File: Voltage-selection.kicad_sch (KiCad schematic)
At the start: 15 parts, among them Q3 DMP1045U-7, Q4 DMP1045U-7, Q5 DMP1045U-7, SW4 6V 300mA

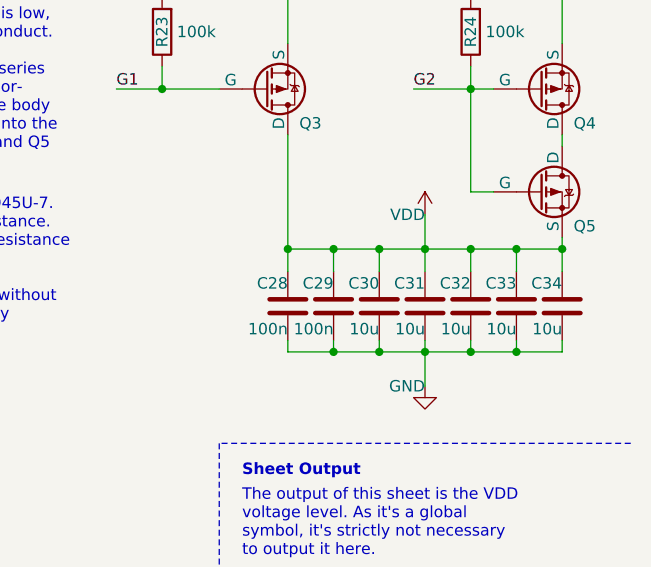
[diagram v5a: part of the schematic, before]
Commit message: Rename capacitors
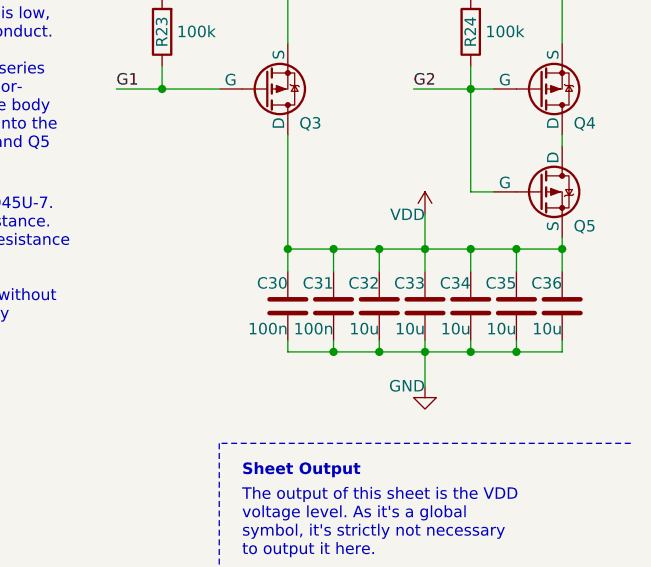
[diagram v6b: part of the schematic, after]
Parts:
- C30: renamed from C28; Comment (none) -> 16V 100nF X7R ±10% 0402
- C31: renamed from C29; Comment (none) -> 16V 100nF X7R ±10% 0402
- C32: renamed from C30; Comment (none) -> 25V 10uF X5R ±10% 0805
- C33: renamed from C31; Comment (none) -> 25V 10uF X5R ±10% 0805
- C34: renamed from C32; Comment (none) -> 25V 10uF X5R ±10% 0805
- C35: renamed from C33; Comment (none) -> 25V 10uF X5R ±10% 0805
- C36: renamed from C34; Comment (none) -> 25V 10uF X5R ±10% 0805
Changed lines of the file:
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@@
   (symbol (lib_id "Device:C") (at 179.07 62.23 0) (mirror y) (unit 1)
     (in_bom yes) (on_board yes) (dnp no)
-    (property "Reference" "C32" (at 179.07 59.69 0)
+    (property "Reference" "C34" (at 179.07 59.69 0)
       (effects (font (size 1.27 1.27)) (justify left))
     )
@@
       (effects (font (size 1.27 1.27)) hide)
     )
+    (property "Comment" "25V 10uF X5R ±10% 0805" (at 179.07 62.23 0)
+      (effects (font (size 1.27 1.27)) hide)
+    )
+    (pin "1")
+    (pin "2")
+    (instances
+      (project "tiny-scarab"
+        (path "/156c5422-ee07-49a4-8263-a2dbd26b90bd/481ed0a2-b40b-451f-8f8b-138317026240"
+          (reference "C34") (unit 1)
+        )
+      )
+    )
+  )
+  (symbol (lib_id "Device:C") (at 168.91 62.23 0) (mirror y) (unit 1)
+    (in_bom yes) (on_board yes) (dnp no)
+    (property "Reference" "C32" (at 168.91 59.69 0)
+      (effects (font (size 1.27 1.27)) (justify left))
+    )
+    (property "Value" "10u" (at 168.91 64.77 0)
+      (effects (font (size 1.27 1.27)) (justify left))
+    )
+    (property "Footprint" "Capacitor_SMD:C_0805_2012Metric" (at 167.9448 66.04 0)
+      (effects (font (size 1.27 1.27)) hide)
+    )
+    (property "Datasheet" "~" (at 168.91 62.23 0)
+      (effects (font (size 1.27 1.27)) hide)
+    )
+    (property "Manufacturer" "Samsung electro-mechanics" (at 168.91 62.23 0)
+      (effects (font (size 1.27 1.27)) hide)
+    )
+    (property "MPN" "CL21A106KAYNNNE" (at 168.91 62.23 0)
+      (effects (font (size 1.27 1.27)) hide)
+    )
+    (property "JLCPCB Part #" "C15850" (at 168.91 62.23 0)
+      (effects (font (size 1.27 1.27)) hide)
+    )
+    (property "Comment" "25V 10uF X5R ±10% 0805" (at 168.91 62.23 0)
+      (effects (font (size 1.27 1.27)) hide)
+    )
     (pin "1")
     (pin "2")
@@
         (path "/156c5422-ee07-49a4-8263-a2dbd26b90bd/481ed0a2-b40b-451f-8f8b-138317026240"
           (reference "C32") (unit 1)
-        )
-      )
-    )
-  )
-  (symbol (lib_id "Device:C") (at 168.91 62.23 0) (mirror y) (unit 1)
-    (in_bom yes) (on_board yes) (dnp no)
-    (property "Reference" "C30" (at 168.91 59.69 0)
-      (effects (font (size 1.27 1.27)) (justify left))
-    )
-    (property "Value" "10u" (at 168.91 64.77 0)
-      (effects (font (size 1.27 1.27)) (justify left))
-    )
-    (property "Footprint" "Capacitor_SMD:C_0805_2012Metric" (at 167.9448 66.04 0)
-      (effects (font (size 1.27 1.27)) hide)
-    )
-    (property "Datasheet" "~" (at 168.91 62.23 0)
-      (effects (font (size 1.27 1.27)) hide)
-    )
-    (property "Manufacturer" "Samsung electro-mechanics" (at 168.91 62.23 0)
-      (effects (font (size 1.27 1.27)) hide)
-    )
-    (property "MPN" "CL21A106KAYNNNE" (at 168.91 62.23 0)
-      (effects (font (size 1.27 1.27)) hide)
-    )
-    (property "JLCPCB Part #" "C15850" (at 168.91 62.23 0)
-      (effects (font (size 1.27 1.27)) hide)
-    )
-    (pin "1")
-    (pin "2")
-    (instances
-      (project "tiny-scarab"
-        (path "/156c5422-ee07-49a4-8263-a2dbd26b90bd/481ed0a2-b40b-451f-8f8b-138317026240"
-          (reference "C30") (unit 1)
         )
       )
@@
   (symbol (lib_id "Device:C") (at 184.15 62.23 0) (mirror y) (unit 1)
     (in_bom yes) (on_board yes) (dnp no)
-    (property "Reference" "C33" (at 184.15 59.69 0)
+    (property "Reference" "C35" (at 184.15 59.69 0)
       (effects (font (size 1.27 1.27)) (justify left))
     )
@@
       (effects (font (size 1.27 1.27)) hide)
     )
-    (pin "1")
-    (pin "2")
-    (instances
-      (project "tiny-scarab"
-        (path "/156c5422-ee07-49a4-8263-a2dbd26b90bd/481ed0a2-b40b-451f-8f8b-138317026240"
-          (reference "C33") (unit 1)
+    (property "Comment" "25V 10uF X5R ±10% 0805" (at 184.15 62.23 0)
+      (effects (font (size 1.27 1.27)) hide)
+    )
+    (pin "1")
+    (pin "2")
+    (instances
+      (project "tiny-scarab"
+        (path "/156c5422-ee07-49a4-8263-a2dbd26b90bd/481ed0a2-b40b-451f-8f8b-138317026240"
+          (reference "C35") (unit 1)
         )
       )
@@
   (symbol (lib_id "Device:C") (at 163.83 62.23 0) (mirror y) (unit 1)
     (in_bom yes) (on_board yes) (dnp no)
-    (property "Reference" "C29" (at 163.83 59.69 0)
+    (property "Reference" "C31" (at 163.83 59.69 0)
       (effects (font (size 1.27 1.27)) (justify left))
     )
@@
       (effects (font (size 1.27 1.27)) hide)
     )
-    (pin "1")
-    (pin "2")
-    (instances
-      (project "tiny-scarab"
-        (path "/156c5422-ee07-49a4-8263-a2dbd26b90bd/481ed0a2-b40b-451f-8f8b-138317026240"
-          (reference "C29") (unit 1)
+    (property "Comment" "16V 100nF X7R ±10% 0402" (at 163.83 62.23 0)
+      (effects (font (size 1.27 1.27)) hide)
+    )
+    (pin "1")
+    (pin "2")
+    (instances
+      (project "tiny-scarab"
+        (path "/156c5422-ee07-49a4-8263-a2dbd26b90bd/481ed0a2-b40b-451f-8f8b-138317026240"
+          (reference "C31") (unit 1)
         )
       )
@@
   (symbol (lib_id "Device:C") (at 189.23 62.23 0) (mirror y) (unit 1)
     (in_bom yes) (on_board yes) (dnp no)
-    (property "Reference" "C34" (at 189.23 59.69 0)
+    (property "Reference" "C36" (at 189.23 59.69 0)
       (effects (font (size 1.27 1.27)) (justify left))
     )
@@
       (effects (font (size 1.27 1.27)) hide)
     )
-    (pin "1")
-    (pin "2")
-    (instances
-      (project "tiny-scarab"
-        (path "/156c5422-ee07-49a4-8263-a2dbd26b90bd/481ed0a2-b40b-451f-8f8b-138317026240"
-          (reference "C34") (unit 1)
+    (property "Comment" "25V 10uF X5R ±10% 0805" (at 189.23 62.23 0)
+      (effects (font (size 1.27 1.27)) hide)
+    )
+    (pin "1")
+    (pin "2")
+    (instances
+      (project "tiny-scarab"
+        (path "/156c5422-ee07-49a4-8263-a2dbd26b90bd/481ed0a2-b40b-451f-8f8b-138317026240"
+          (reference "C36") (unit 1)
         )
       )
@@
   (symbol (lib_id "Device:C") (at 158.75 62.23 0) (mirror y) (unit 1)
     (in_bom yes) (on_board yes) (dnp no)
-    (property "Reference" "C28" (at 158.75 59.69 0)
+    (property "Reference" "C30" (at 158.75 59.69 0)
       (effects (font (size 1.27 1.27)) (justify left))
     )
@@
       (effects (font (size 1.27 1.27)) hide)
     )
-    (pin "1")
-    (pin "2")
-    (instances
-      (project "tiny-scarab"
-        (path "/156c5422-ee07-49a4-8263-a2dbd26b90bd/481ed0a2-b40b-451f-8f8b-138317026240"
-          (reference "C28") (unit 1)
+    (property "Comment" "16V 100nF X7R ±10% 0402" (at 158.75 62.23 0)
+      (effects (font (size 1.27 1.27)) hide)
+    )
+    (pin "1")
+    (pin "2")
+    (instances
+      (project "tiny-scarab"
+        (path "/156c5422-ee07-49a4-8263-a2dbd26b90bd/481ed0a2-b40b-451f-8f8b-138317026240"
+          (reference "C30") (unit 1)
         )
       )
@@
   (symbol (lib_id "Device:C") (at 173.99 62.23 0) (mirror y) (unit 1)
     (in_bom yes) (on_board yes) (dnp no)
-    (property "Reference" "C31" (at 173.99 59.69 0)
+    (property "Reference" "C33" (at 173.99 59.69 0)
       (effects (font (size 1.27 1.27)) (justify left))
     )
@@
       (effects (font (size 1.27 1.27)) hide)
     )
-    (pin "1")
-    (pin "2")
-    (instances
-      (project "tiny-scarab"
-        (path "/156c5422-ee07-49a4-8263-a2dbd26b90bd/481ed0a2-b40b-451f-8f8b-138317026240"
-          (reference "C31") (unit 1)
-        )
-      )
+    (property "Comment" "25V 10uF X5R ±10% 0805" (at 173.99 62.23 0)
+      (effects (font (size 1.27 1.27)) hide)
+    )
+    (pin "1")
+    (pin "2")
+    (instances
+      (project "tiny-scarab"
+        (path "/156c5422-ee07-49a4-8263-a2dbd26b90bd/481ed0a2-b40b-451f-8f8b-138317026240"
+          (reference "C33") (unit 1)
+        )
+      )

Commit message: Update parts
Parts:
- removed SW4: 6V 300mA, Tiny_Scarab:SW_Slide_SPDT_ALPSALPINE_SSSS2, symbol Tiny_Scarab:SW_SSSS213202
- added SW4: 12V 50mA, Tiny_Scarab:SW_Slide_SPDT_XKB-Connectivity_SS-3235D-03-L3, symbol Tiny_Scarab:SW_SS-3235D-03-L3
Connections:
- net G1: now also SW4.1 (A)
- net G2: now also SW4.3 (C)
- net GND: now also SW4.2 (B)
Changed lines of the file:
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@@
-    )
-  )
-  (symbol (lib_id "Tiny_Scarab:SW_SSSS213202") (at 69.85 38.1 0) (mirror x) (unit 1)
-    (in_bom yes) (on_board yes) (dnp no)
-    (property "Reference" "SW4" (at 68.58 35.56 0)
-      (effects (font (size 1.27 1.27)))
-    )
-    (property "Value" "6V 300mA" (at 69.85 33.02 0)
-      (effects (font (size 1.27 1.27)) hide)
-    )
-    (property "Footprint" "Tiny_Scarab:SW_Slide_SPDT_ALPSALPINE_SSSS2" (at 69.85 62.23 0)
-      (effects (font (size 1.27 1.27)) hide)
-    )
-    (property "Datasheet" "https://www.farnell.com/datasheets/2864486.pdf" (at 69.85 59.69 0)
-      (effects (font (size 1.27 1.27)) hide)
-    )
-    (property "Manufacturer" "ALPSALPINE" (at 69.85 57.15 0)
-      (effects (font (size 1.27 1.27)) hide)
-    )
-    (property "MPN" "SSSS213202" (at 69.85 54.61 0)
-      (effects (font (size 1.27 1.27)) hide)
-    )
-    (property "JLCPCB Part #" "C115375" (at 69.85 52.07 0)
-      (effects (font (size 1.27 1.27)) hide)
-    )
-    (property "DigiKey" "" (at 69.85 38.1 0)
-      (effects (font (size 1.27 1.27)) hide)
-    )
-    (property "Farnell" "3261782" (at 69.85 49.53 0)
-      (effects (font (size 1.27 1.27)) hide)
-    )
-    (property "Mouser" "688-SSSS213202" (at 69.85 46.99 0)
-      (effects (font (size 1.27 1.27)) hide)
-    )
-    (pin "3")
-    (pin "2")
-    (pin "1")
-    (instances
-      (project "tiny-scarab"
-        (path "/156c5422-ee07-49a4-8263-a2dbd26b90bd/481ed0a2-b40b-451f-8f8b-138317026240"
-          (reference "SW4") (unit 1)
-        )
-      )
     )
   )
@@
         )
       )
+    )
+  )
+  (symbol (lib_id "Tiny_Scarab:SW_SS-3235D-03-L3") (at 69.85 38.1 0) (unit 1)
+    (in_bom yes) (on_board yes) (dnp no) (fields_autoplaced)
+    (property "Reference" "SW4" (at 69.85 30.48 0)
+      (effects (font (size 1.27 1.27)))
+    )
+    (property "Value" "12V 50mA" (at 69.85 33.02 0)
+      (effects (font (size 1.27 1.27)))
+    )
+    (property "Footprint" "Tiny_Scarab:SW_Slide_SPDT_XKB-Connectivity_SS-3235D-03-L3" (at 69.85 13.97 0)
+      (effects (font (size 1.27 1.27)) hide)
+    )
+    (property "Datasheet" "" (at 69.85 16.51 0)
+      (effects (font (size 1.27 1.27)) hide)
+    )
+    (property "Manufacturer" "XKB Connectivity" (at 69.85 19.05 0)
+      (effects (font (size 1.27 1.27)) hide)
+    )
+    (property "MPN" "SS-3235D-03-L3" (at 69.85 21.59 0)
+      (effects (font (size 1.27 1.27)) hide)
+    )
+    (property "JLCPCB Part #" "C2884764" (at 69.85 24.13 0)
+      (effects (font (size 1.27 1.27)) hide)
+    )
+    (property "DigiKey" "" (at 69.85 38.1 0)
+      (effects (font (size 1.27 1.27)) hide)
+    )
+    (property "Farnell" "" (at 69.85 26.67 0)
+      (effects (font (size 1.27 1.27)) hide)
+    )
+    (property "Mouser" "" (at 69.85 29.21 0)
+      (effects (font (size 1.27 1.27)) hide)
+    )
+    (pin "1")
+    (pin "2")
+    (pin "3")
+    (instances
+      (project "tiny-scarab"
+        (path "/156c5422-ee07-49a4-8263-a2dbd26b90bd/481ed0a2-b40b-451f-8f8b-138317026240"
+          (reference "SW4") (unit 1)
+        )
+      )

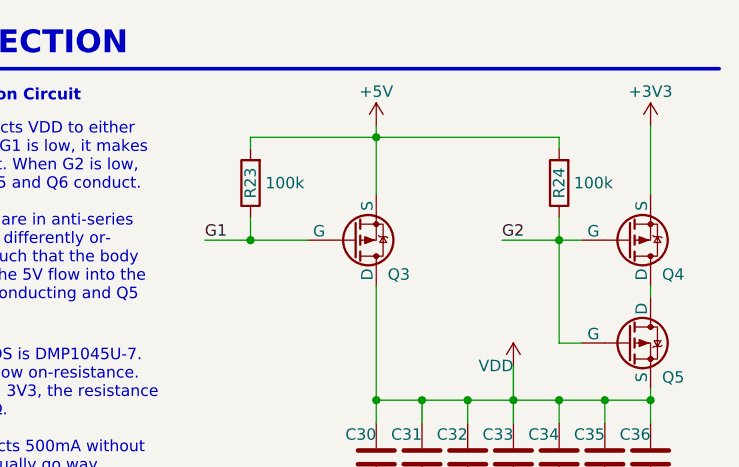
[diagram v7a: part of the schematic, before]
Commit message: Modify resistors for LEDs
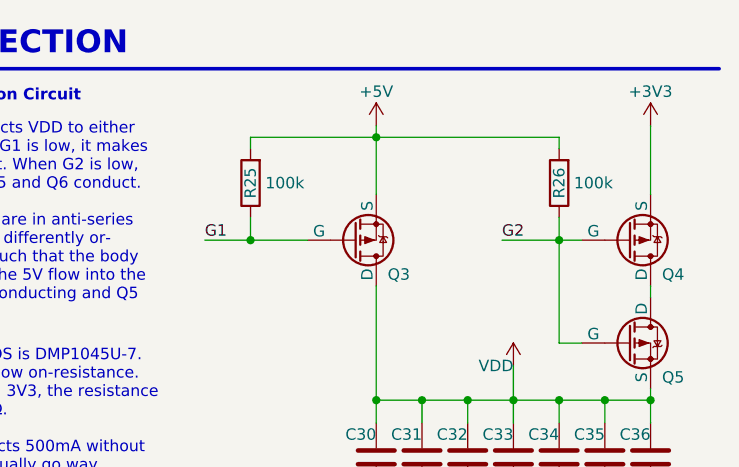
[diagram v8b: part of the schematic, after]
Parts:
- renumbered R23 to R25, R24 to R26
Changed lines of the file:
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@@
   (symbol (lib_id "Device:R") (at 144.78 31.75 180) (unit 1)
     (in_bom yes) (on_board yes) (dnp no)
-    (property "Reference" "R23" (at 144.78 31.75 90)
+    (property "Reference" "R25" (at 144.78 31.75 90)
       (effects (font (size 1.27 1.27)))
     )
@@
       (project "tiny-scarab"
         (path "/156c5422-ee07-49a4-8263-a2dbd26b90bd/481ed0a2-b40b-451f-8f8b-138317026240"
-          (reference "R23") (unit 1)
+          (reference "R25") (unit 1)
         )
       )
@@
   (symbol (lib_id "Device:R") (at 179.07 31.75 180) (unit 1)
     (in_bom yes) (on_board yes) (dnp no)
-    (property "Reference" "R24" (at 179.07 31.75 90)
+    (property "Reference" "R26" (at 179.07 31.75 90)
       (effects (font (size 1.27 1.27)))
     )
@@
       (project "tiny-scarab"
         (path "/156c5422-ee07-49a4-8263-a2dbd26b90bd/481ed0a2-b40b-451f-8f8b-138317026240"
-          (reference "R24") (unit 1)
-        )
-      )
+          (reference "R26") (unit 1)
+        )
+      )
